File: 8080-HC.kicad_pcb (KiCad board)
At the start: 4 copper layers, 352 parts, among them U1 74HCU04, U10 74HC00, U11 74HC126, U12 74HC161, U13 74HC238, U14 74HC238, U15 74HC238, U16 74HC238, U17 74HC04, U178 74LS03, U18 74HC05, U181 74HC244, U182 74HC244, U19 74HC74, U194 74HC244, U195 74HC244, U2 74HC74, U20 74HC373, U21 74HC373, U215 74HC193, U216 74HC193, U217 74HC193, U218 74HC193, U22 74HC373, U23 74HC373, U231 74HC245, U232 74HC04, U233 74HC04, U234 74LS373, U239 74HC74, U24 74HC373, U242 74HC00, U243 74HCU04, U244 74HC00, U25 74HC244, U26 74HC244, U27 74HC244, U28 74HC244, U29 74HC244, U3 74HC00, U30 74HC373, U31 74HC373, U32 74HC244, U33 74HC244, U34 74HC244, U35 74HC244, U36 74HC373, U37 74HC373, U38 74HC244, U39 74HC244, U4 74HC04, U40 74HC244, U41 74HC244, U43 74HC04, U44 74HC04, U46 74HC04, U47 74HC04, U48 74HC04, U49 74HC04, U5 74HC00, U50 74HC04, U51 74HC04, U52 74HC04, U53 74HC238, U54 74HC238, U55 74HC238, U56 74HC238, U57 74HC04, U58 74HC04, U6 74HC04, U69 74HC05, U7 74HC05, U70 74LS05, U71 74HC04, U72 74LS126, U73 74LS126, U74 74LS126, U75 74LS126, U76 74LS126, U77 74HC00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

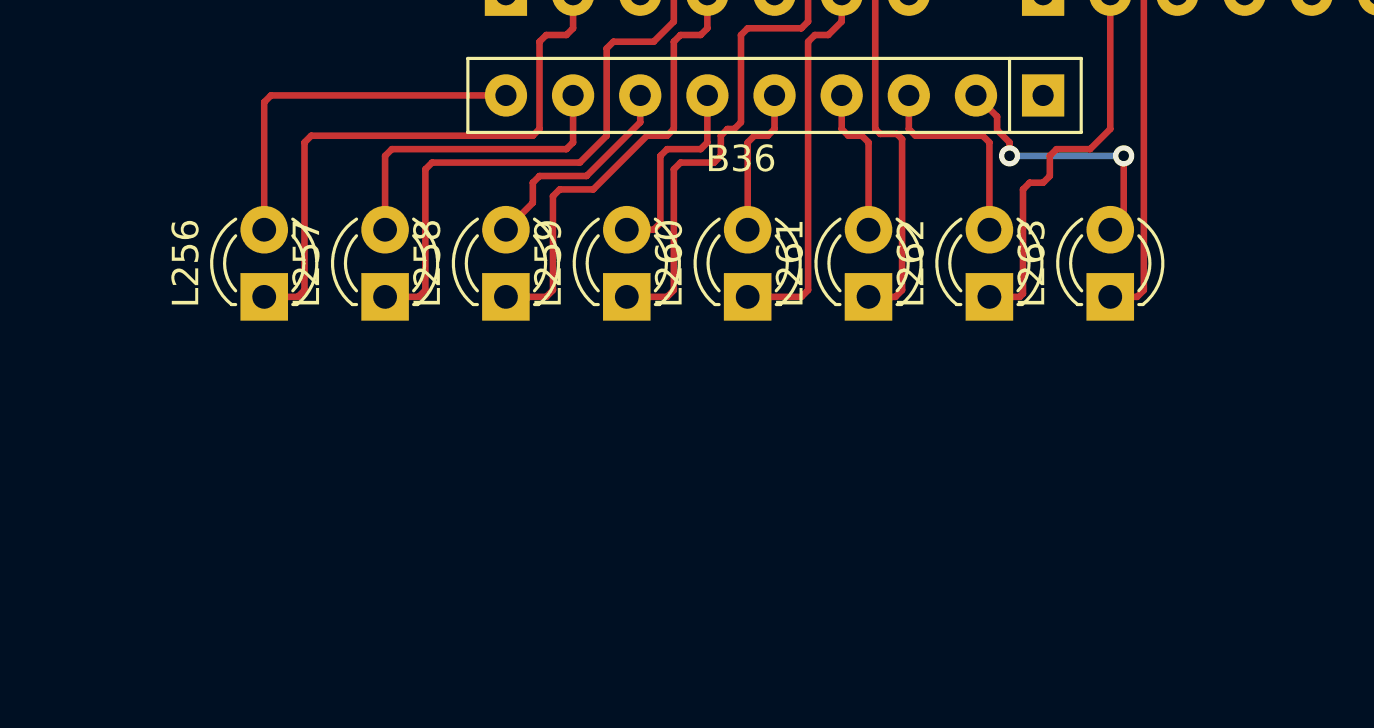
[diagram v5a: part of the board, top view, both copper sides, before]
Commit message: finished Inner BUS, added screenshot
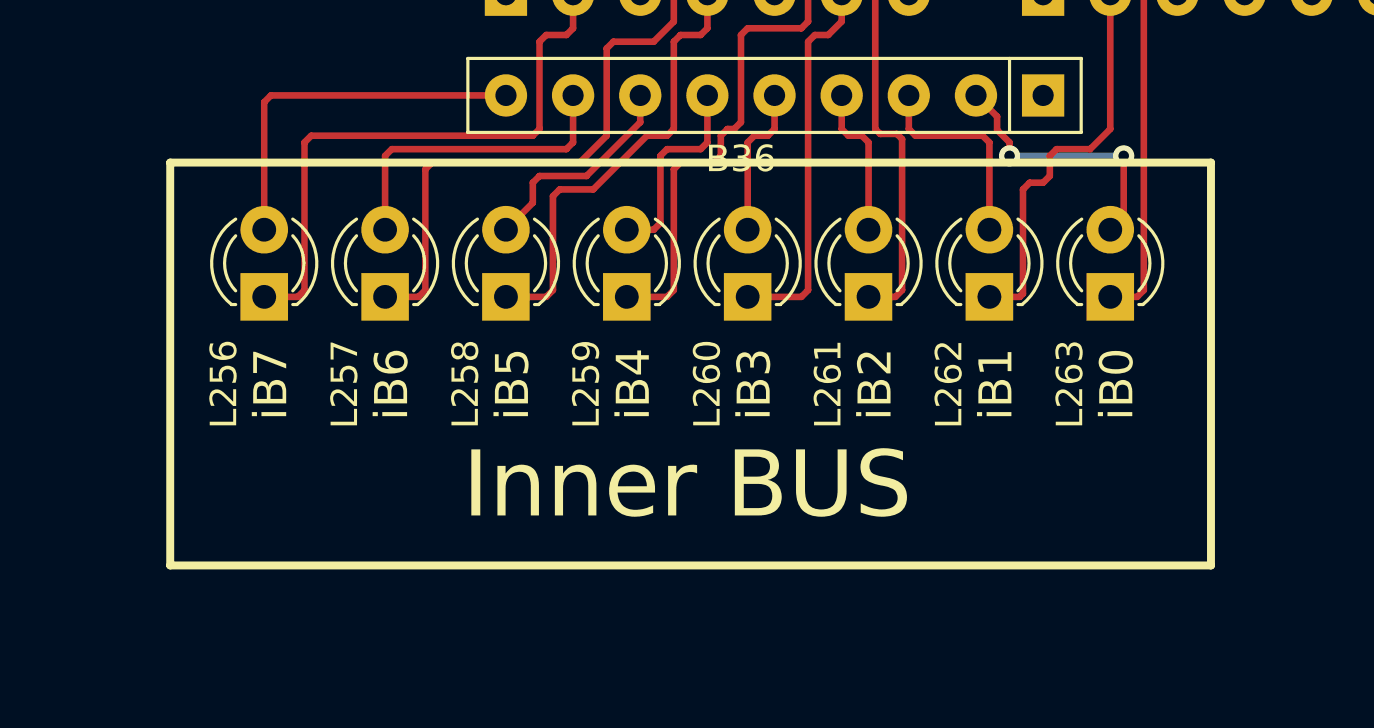
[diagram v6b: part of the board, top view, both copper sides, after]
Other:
- board text added: "Inner BUS"
- board text added: "iB0"
- board text added: "iB1"
- board text added: "iB2"
- board text added: "iB3"
- board text added: "iB4"
- board text added: "iB5"
- board text added: "iB6"
- board text added: "iB7"
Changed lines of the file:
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@@
   (general
     (thickness 1.6)
-    (drawings 40)
+    (drawings 53)
     (tracks 1317)
     (zones 0)
@@
     (descr "LED, diameter 3.0mm, 2 pins")
     (tags "LED diameter 3.0mm 2 pins")
-    (fp_text reference L256 (at 1.27 -2.96 90) (layer F.SilkS)
+    (fp_text reference L256 (at -3.302 -1.524 90) (layer F.SilkS)
       (effects (font (size 1 1) (thickness 0.15)))
     )
@@
     (descr "LED, diameter 3.0mm, 2 pins")
     (tags "LED diameter 3.0mm 2 pins")
-    (fp_text reference L257 (at 1.27 -2.96 90) (layer F.SilkS)
+    (fp_text reference L257 (at -3.302 -1.524 90) (layer F.SilkS)
       (effects (font (size 1 1) (thickness 0.15)))
     )
@@
     (descr "LED, diameter 3.0mm, 2 pins")
     (tags "LED diameter 3.0mm 2 pins")
-    (fp_text reference L258 (at 1.27 -2.96 90) (layer F.SilkS)
+    (fp_text reference L258 (at -3.302 -1.524 90) (layer F.SilkS)
       (effects (font (size 1 1) (thickness 0.15)))
     )
@@
     (descr "LED, diameter 3.0mm, 2 pins")
     (tags "LED diameter 3.0mm 2 pins")
-    (fp_text reference L259 (at 1.27 -2.96 90) (layer F.SilkS)
+    (fp_text reference L259 (at -3.302 -1.524 90) (layer F.SilkS)
       (effects (font (size 1 1) (thickness 0.15)))
     )
@@
     (descr "LED, diameter 3.0mm, 2 pins")
     (tags "LED diameter 3.0mm 2 pins")
-    (fp_text reference L260 (at 1.27 -2.96 90) (layer F.SilkS)
+    (fp_text reference L260 (at -3.302 -1.524 90) (layer F.SilkS)
       (effects (font (size 1 1) (thickness 0.15)))
     )
@@
     (descr "LED, diameter 3.0mm, 2 pins")
     (tags "LED diameter 3.0mm 2 pins")
-    (fp_text reference L261 (at 1.27 -2.96 90) (layer F.SilkS)
+    (fp_text reference L261 (at -3.302 -1.524 90) (layer F.SilkS)
       (effects (font (size 1 1) (thickness 0.15)))
     )
@@
     (descr "LED, diameter 3.0mm, 2 pins")
     (tags "LED diameter 3.0mm 2 pins")
-    (fp_text reference L262 (at 1.27 -2.96 90) (layer F.SilkS)
+    (fp_text reference L262 (at -3.302 -1.524 90) (layer F.SilkS)
       (effects (font (size 1 1) (thickness 0.15)))
     )
@@
     (descr "LED, diameter 3.0mm, 2 pins")
     (tags "LED diameter 3.0mm 2 pins")
-    (fp_text reference L263 (at 1.27 -2.96 90) (layer F.SilkS)
+    (fp_text reference L263 (at -3.302 -1.524 90) (layer F.SilkS)
       (effects (font (size 1 1) (thickness 0.15)))
     )
@@
     )
   )
+  (gr_line (start -228.6 3.81) (end -228.6 -11.43) (layer F.SilkS) (width 0.3))
+  (gr_line (start -189.23 3.81) (end -228.6 3.81) (layer F.SilkS) (width 0.3))
+  (gr_line (start -189.23 -11.43) (end -189.23 3.81) (layer F.SilkS) (width 0.3))
+  (gr_line (start -228.6 -11.43) (end -189.23 -11.43) (layer F.SilkS) (width 0.3))
+  (gr_text "Inner BUS" (at -209.042 0.762) (layer F.SilkS)
+    (effects (font (size 2.5 2.5) (thickness 0.4)))
+  )
+  (gr_text iB0 (at -192.786 -3.048 90) (layer F.SilkS)
+    (effects (font (size 1.25 1.25) (thickness 0.15)))
+  )
+  (gr_text iB1 (at -197.358 -3.048 90) (layer F.SilkS)
+    (effects (font (size 1.25 1.25) (thickness 0.15)))
+  )
+  (gr_text iB2 (at -201.93 -3.048 90) (layer F.SilkS)
+    (effects (font (size 1.25 1.25) (thickness 0.15)))
+  )
+  (gr_text iB3 (at -206.502 -3.048 90) (layer F.SilkS)
+    (effects (font (size 1.25 1.25) (thickness 0.15)))
+  )
+  (gr_text iB4 (at -211.074 -3.048 90) (layer F.SilkS)
+    (effects (font (size 1.25 1.25) (thickness 0.15)))
+  )
+  (gr_text iB5 (at -215.646 -3.048 90) (layer F.SilkS)
+    (effects (font (size 1.25 1.25) (thickness 0.15)))
+  )
+  (gr_text iB6 (at -220.218 -3.048 90) (layer F.SilkS)
+    (effects (font (size 1.25 1.25) (thickness 0.15)))
+  )
+  (gr_text iB7 (at -224.79 -3.048 90) (layer F.SilkS)
+    (effects (font (size 1.25 1.25) (thickness 0.15)))
+  )
   (gr_text OP0 (at -141.732 -15.748 90) (layer F.SilkS)
